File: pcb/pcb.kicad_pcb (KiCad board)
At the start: 2 copper layers, 76.5 x 91.5 mm, 15 parts, among them U1 LD1117S33TR_SOT223

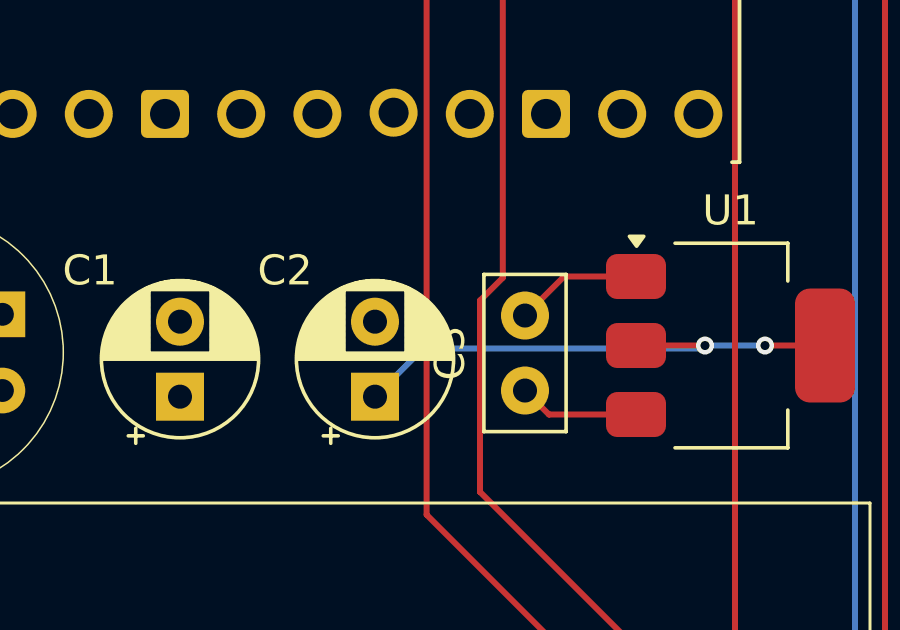
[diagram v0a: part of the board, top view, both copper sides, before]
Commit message: feat: dt rather than fps
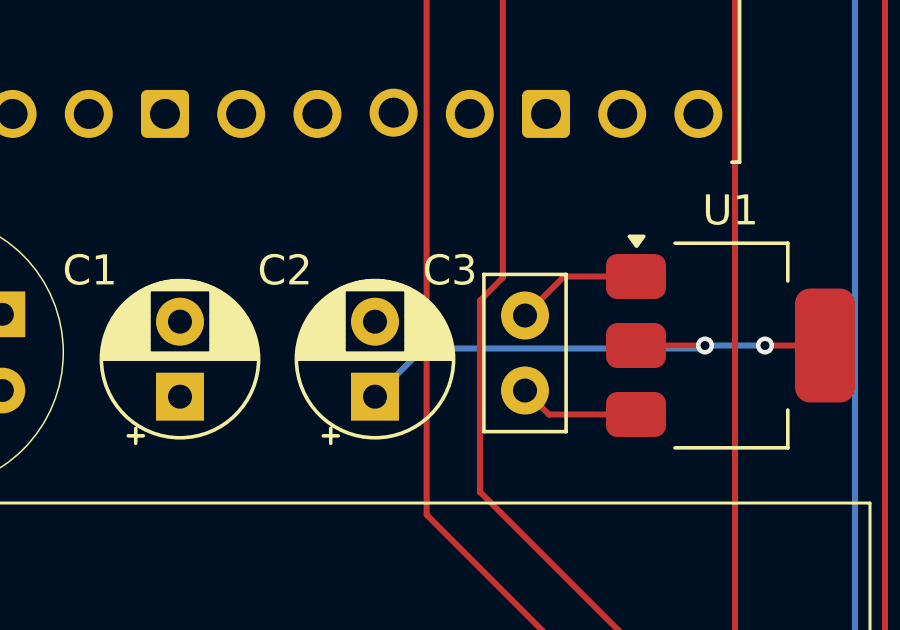
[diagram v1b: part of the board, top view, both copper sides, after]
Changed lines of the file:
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@@
 		(tags "C Disc series Radial pin pitch 2.50mm  diameter 5mm width 2.5mm Capacitor")
 		(property "Reference" "C3"
-			(at 1.25 -2.5 90)
+			(at 4 -2.5 180)
 			(layer "F.SilkS")
 			(effects
